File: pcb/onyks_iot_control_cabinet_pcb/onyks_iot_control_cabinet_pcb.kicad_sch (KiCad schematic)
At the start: 4 parts

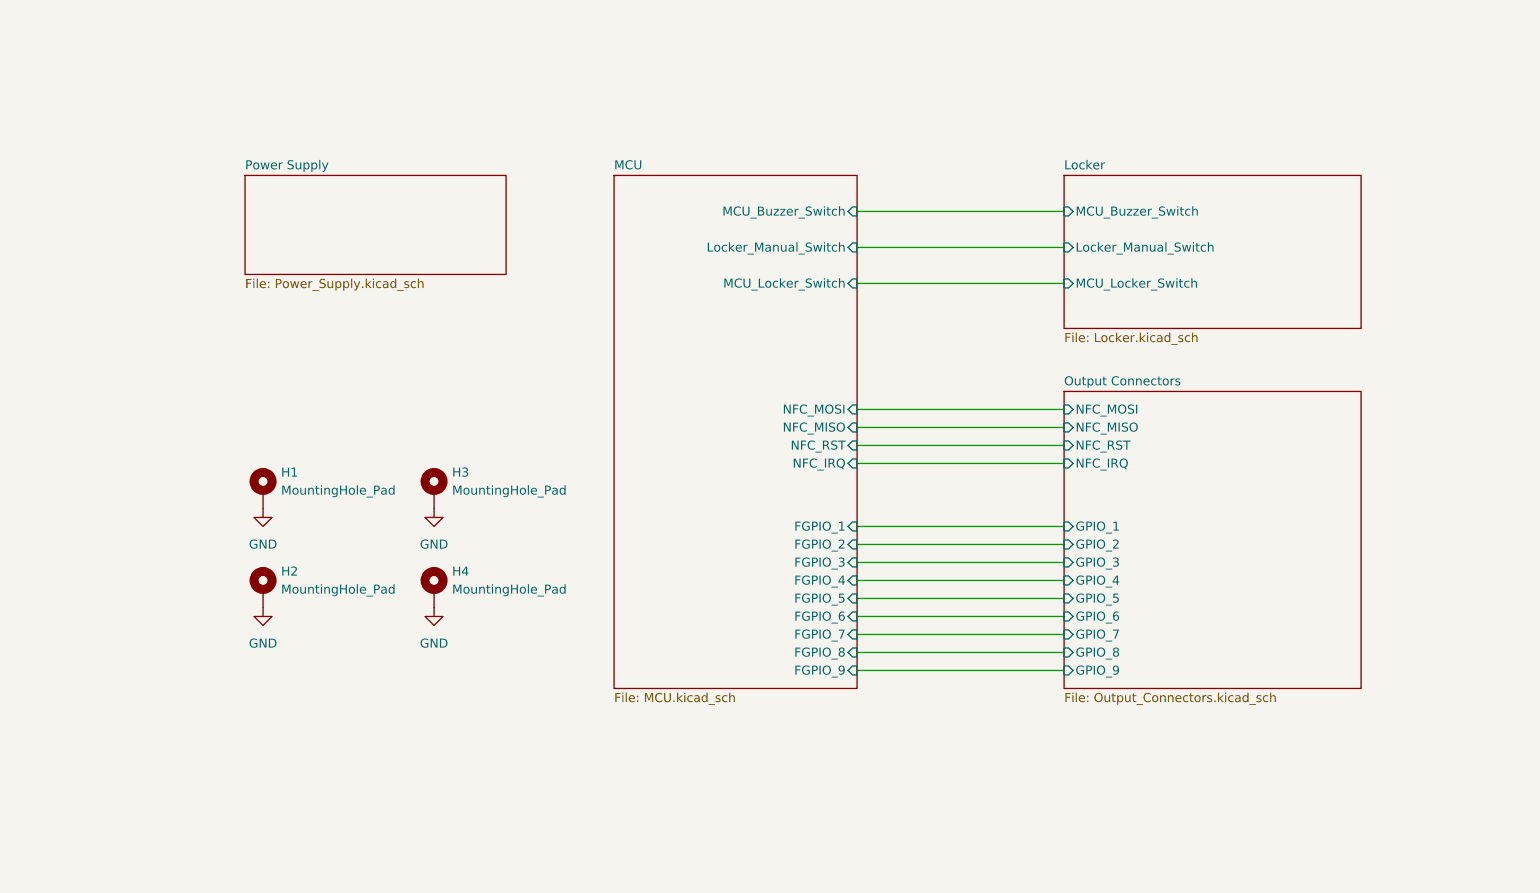
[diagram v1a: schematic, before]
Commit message: Update of the power supply and added the header for 125kHz RFID
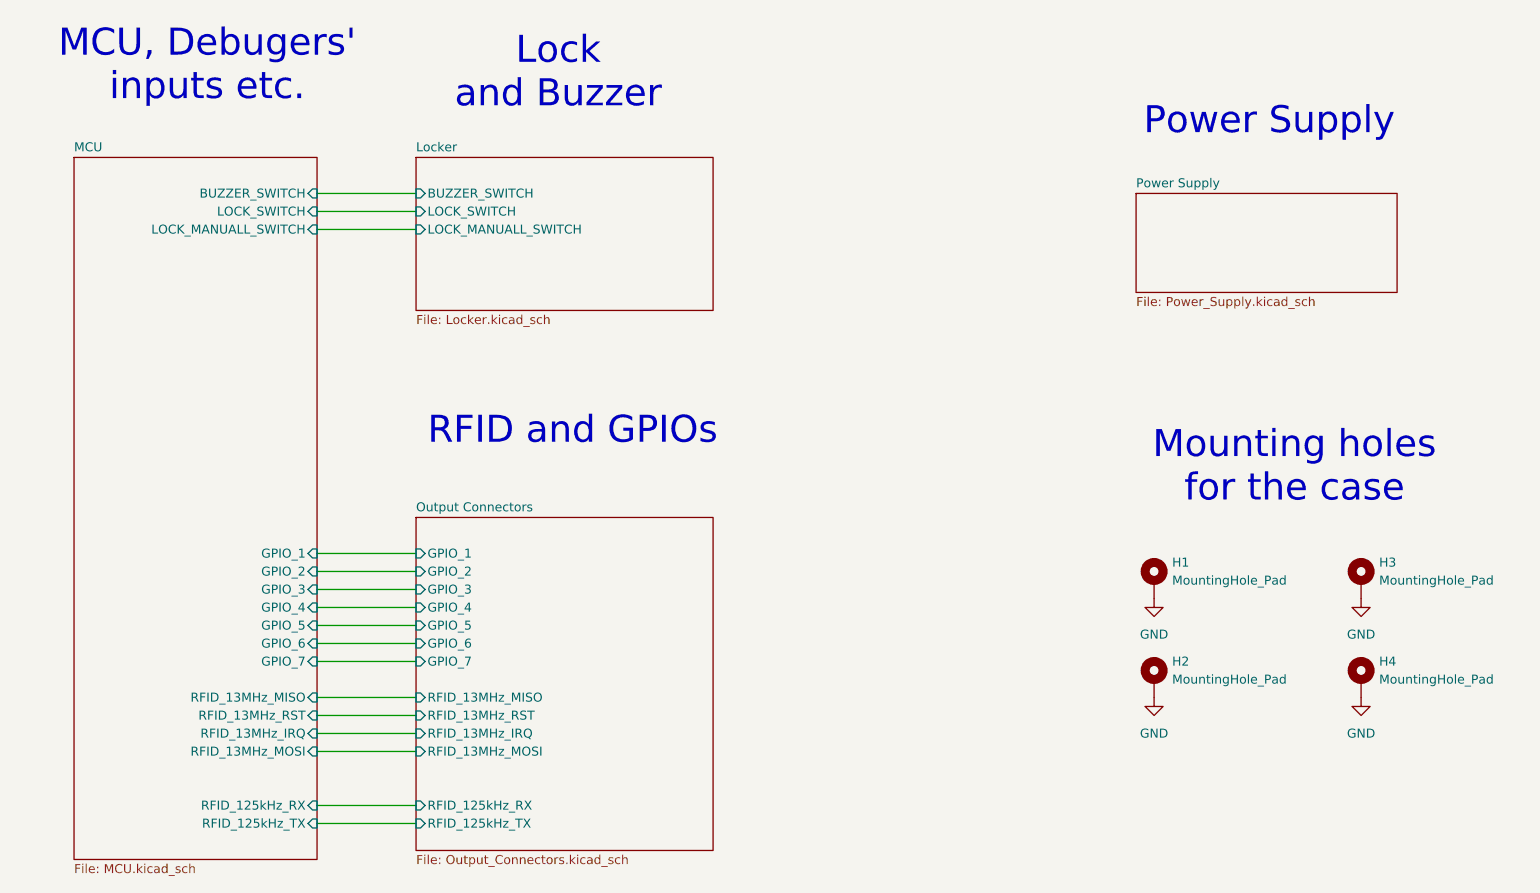
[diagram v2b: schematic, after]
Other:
- sheet Locker ports: added BUZZER_SWITCH, LOCK_MANUALL_SWITCH, LOCK_SWITCH; removed Locker_Manual_Switch, MCU_Buzzer_Switch, MCU_Locker_Switch
- sheet MCU ports: added BUZZER_SWITCH, GPIO_1, GPIO_2, GPIO_3, GPIO_4, GPIO_5, GPIO_6, GPIO_7, LOCK_MANUALL_SWITCH, LOCK_SWITCH, RFID_125kHz_RX, RFID_125kHz_TX, RFID_13MHz_IRQ, RFID_13MHz_MISO, RFID_13MHz_MOSI, RFID_13MHz_RST; removed FGPIO_1, FGPIO_2, FGPIO_3, FGPIO_4, FGPIO_5, FGPIO_6, FGPIO_7, FGPIO_8, FGPIO_9, Locker_Manual_Switch, MCU_Buzzer_Switch, MCU_Locker_Switch, NFC_IRQ, NFC_MISO, NFC_MOSI, NFC_RST
- sheet Output Connectors ports: added RFID_125kHz_RX, RFID_125kHz_TX, RFID_13MHz_IRQ, RFID_13MHz_MISO, RFID_13MHz_MOSI, RFID_13MHz_RST; removed GPIO_8, GPIO_9, NFC_IRQ, NFC_MISO, NFC_MOSI, NFC_RST
- note added: "Lock and Buzzer"
- note added: "MCU, Debugers' inputs etc."
- note added: "Mounting holes for the case"
- note added: "Power Supply"
- note added: "RFID and GPIOs"
- moved on the sheet: H1, H2, H3, H4

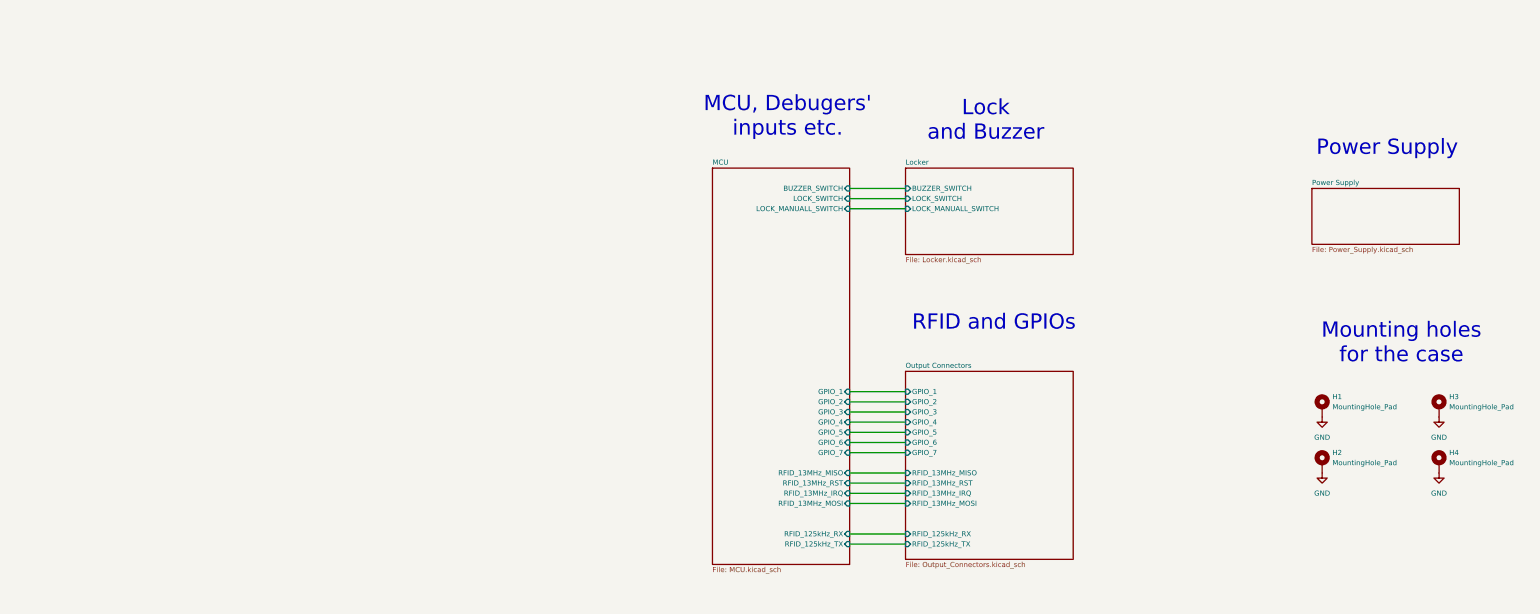
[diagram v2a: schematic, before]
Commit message: Schematics update; power supply and footprints fixes
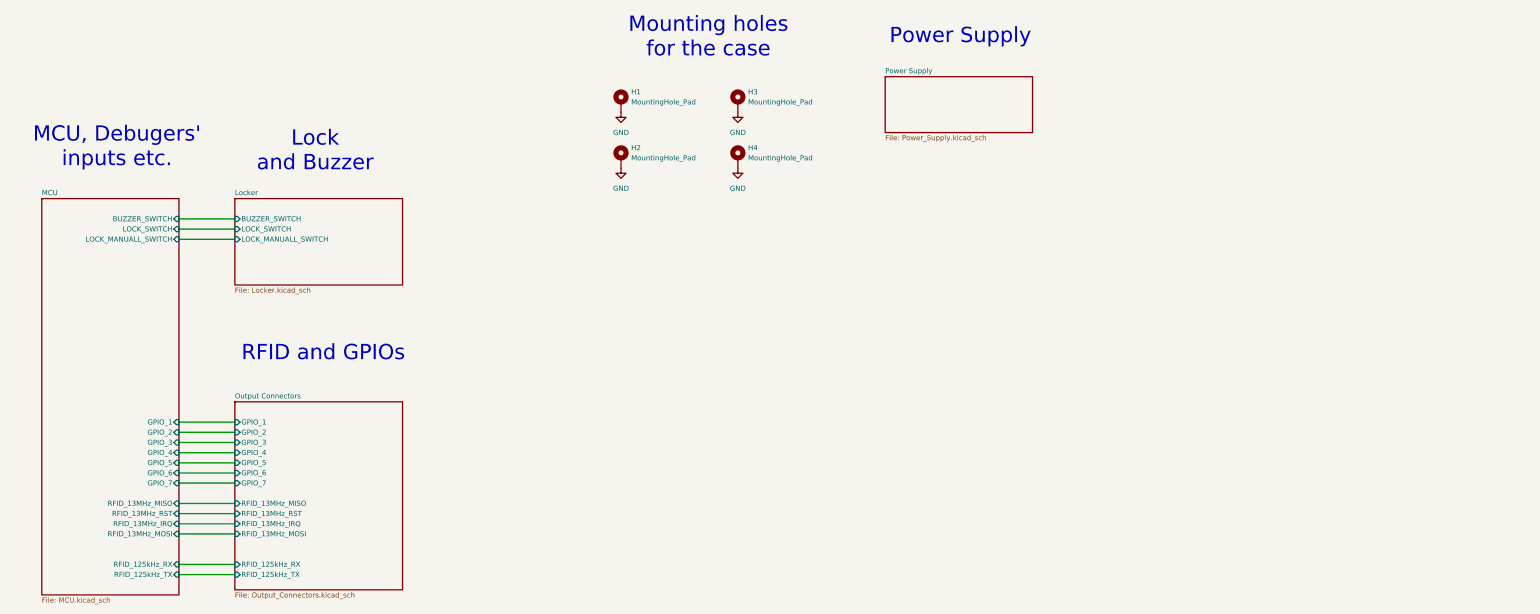
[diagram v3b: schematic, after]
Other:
- moved on the sheet: H1, H2, H3, H4

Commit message: PCB Ressurection
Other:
- moved on the sheet: H1, H2, H3, H4

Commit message: PCB Update
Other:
- sheet MCU ports: added GPIO_O1, GPIO_O2, GPIO_O3, GPIO_O4, GPIO_O5, GPIO_O6, GPIO_O7; removed GPIO_1, GPIO_2, GPIO_3, GPIO_4, GPIO_5, GPIO_6, GPIO_7
- sheet Output Connectors ports: added GPIO_O1, GPIO_O2, GPIO_O3, GPIO_O4, GPIO_O5, GPIO_O6, GPIO_O7; removed GPIO_1, GPIO_2, GPIO_3, GPIO_4, GPIO_5, GPIO_6, GPIO_7
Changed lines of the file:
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@@
 			)
 		)
-		(pin "GPIO_7" input
+		(pin "GPIO_O7" input
 			(at 67.31 129.54 0)
 			(effects
@@
 			)
 		)
-		(pin "GPIO_2" input
+		(pin "GPIO_O2" input
 			(at 67.31 116.84 0)
 			(effects
@@
 			)
 		)
-		(pin "GPIO_3" input
+		(pin "GPIO_O3" input
 			(at 67.31 119.38 0)
 			(effects
@@
 			)
 		)
-		(pin "GPIO_1" input
+		(pin "GPIO_O1" input
 			(at 67.31 114.3 0)
 			(effects
@@
 			)
 		)
-		(pin "GPIO_4" input
+		(pin "GPIO_O4" input
 			(at 67.31 121.92 0)
 			(effects
@@
 			)
 		)
-		(pin "GPIO_6" input
+		(pin "GPIO_O6" input
 			(at 67.31 127 0)
 			(effects
@@
 			)
 		)
-		(pin "GPIO_5" input
+		(pin "GPIO_O5" input
 			(at 67.31 124.46 0)
 			(effects
@@
 			)
 		)
-		(pin "GPIO_6" input
+		(pin "GPIO_O6" input
 			(at 104.14 127 180)
 			(effects
@@
 			)
 		)
-		(pin "GPIO_7" input
+		(pin "GPIO_O7" input
 			(at 104.14 129.54 180)
 			(effects
@@
 			)
 		)
-		(pin "GPIO_5" input
+		(pin "GPIO_O5" input
 			(at 104.14 124.46 180)
 			(effects
@@
 			)
 		)
-		(pin "GPIO_2" input
+		(pin "GPIO_O2" input
 			(at 104.14 116.84 180)
 			(effects
@@
 			)
 		)
-		(pin "GPIO_4" input
+		(pin "GPIO_O4" input
 			(at 104.14 121.92 180)
 			(effects
@@
 			)
 		)
-		(pin "GPIO_3" input
+		(pin "GPIO_O3" input
 			(at 104.14 119.38 180)
 			(effects
@@
 			)
 		)
-		(pin "GPIO_1" input
+		(pin "GPIO_O1" input
 			(at 104.14 114.3 180)
 			(effects
